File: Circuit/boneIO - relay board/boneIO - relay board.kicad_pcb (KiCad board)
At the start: 2 copper layers, 169 x 102 mm, 47 parts, among them J1 Screw_Terminal_01x04, J10 Screw_Terminal_01x04, J11 Screw_Terminal_01x04, J12 Conn_02x13_Odd_Even, J2 Screw_Terminal_01x04, J3 Screw_Terminal_01x04, J4 Screw_Terminal_01x04, J5 Screw_Terminal_01x04, J6 Screw_Terminal_01x04, J7 POWER RELAY, J8 Screw_Terminal_01x04, J9 Screw_Terminal_01x04, K1 RM85-2011-35-1005, K10 RM85-2011-35-1005, K11 RM85-2011-35-1005, K12 RM85-2011-35-1005, K13 RM85-2011-35-1005, K14 RM85-2011-35-1005, K15 RM85-2011-35-1005, K16 RM85-2011-35-1005, K17 RM85-2011-35-1005, K18 RM85-2011-35-1005, K19 RM85-2011-35-1005, K2 RM85-2011-35-1005, K20 RM85-2011-35-1005, K3 RM85-2011-35-1005, K4 RM85-2011-35-1005, K5 RM85-2011-35-1005, K6 RM85-2011-35-1005, K7 RM85-2011-35-1005, K8 RM85-2011-35-1005, K9 RM85-2011-35-1005, U1 ULN2803A, U2 ULN2803A, U3 ULN2803A, U4 MCP9808_MSOP

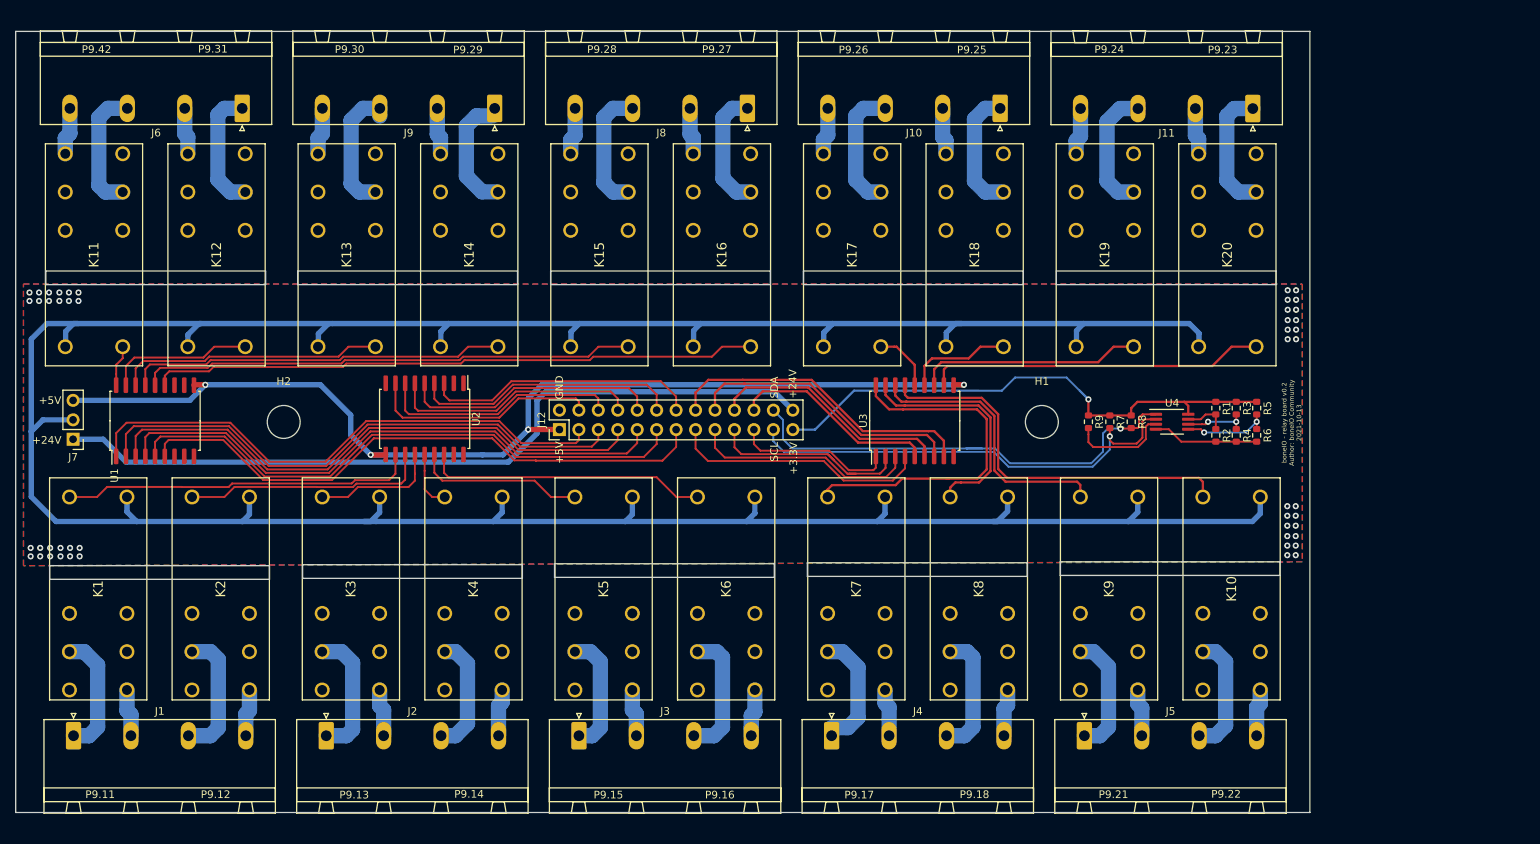
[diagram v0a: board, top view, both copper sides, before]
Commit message: Circuit Repo Cleanup
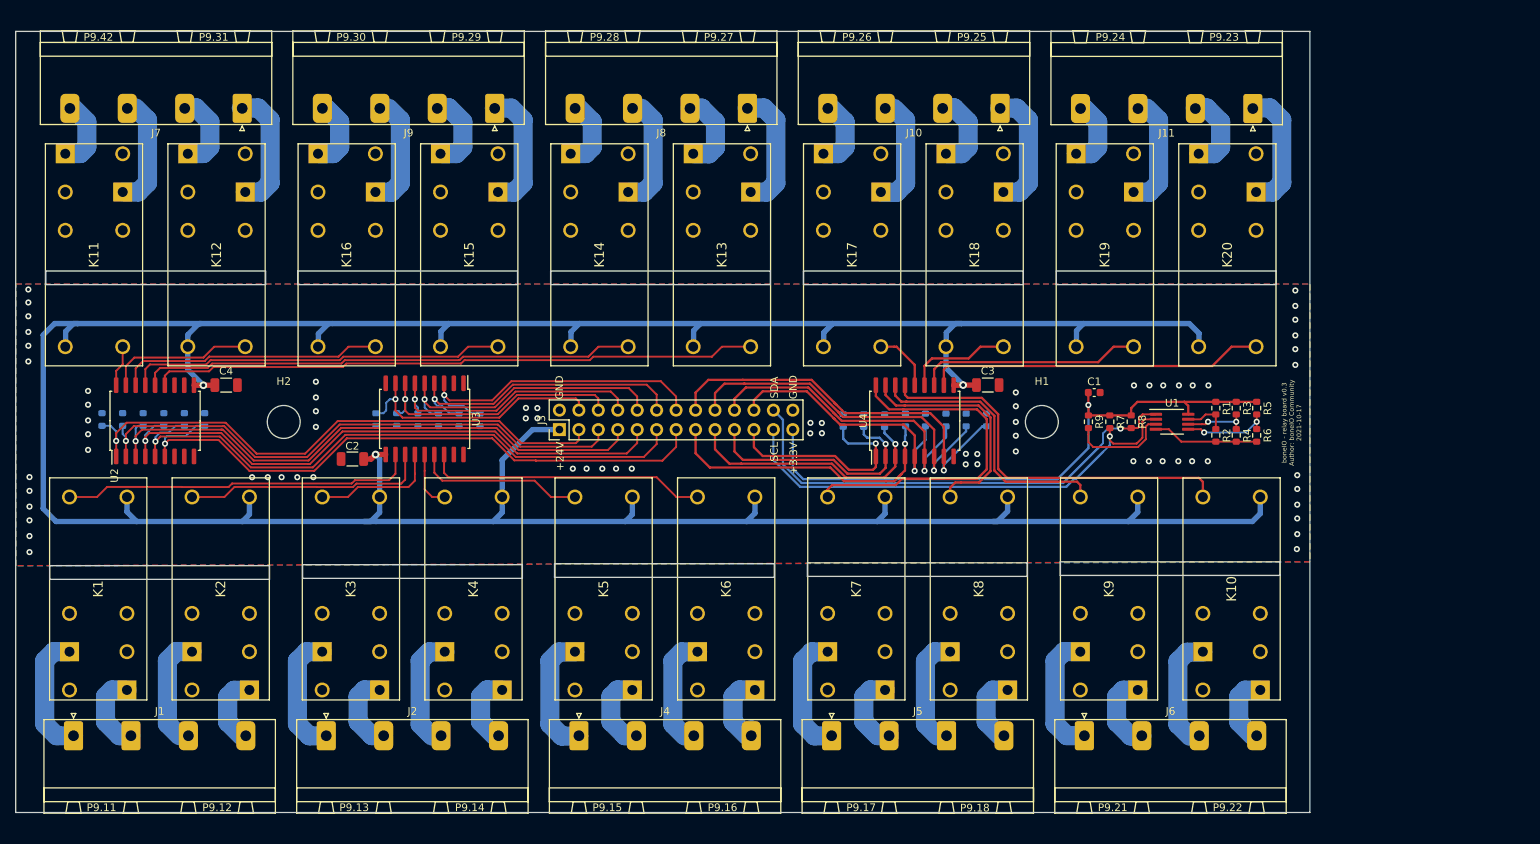
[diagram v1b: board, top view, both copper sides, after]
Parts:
- removed the J7 at (295.6, 317.0)
- added C1: 100n, Capacitor_SMD:C_0603_1608Metric, F.Cu at (429.0, 310.9)
- added C2: 4.7uF/50V, Capacitor_SMD:C_1206_3216Metric, F.Cu at (332.1, 319.5)
- added C3: 4.7uF/50V, Capacitor_SMD:C_1206_3216Metric, F.Cu at (415.1, 309.9)
- added C4: 4.7uF/50V, Capacitor_SMD:C_1206_3216Metric, F.Cu at (315.6, 309.9)
- added R10: 10k, Resistor_SMD:R_0603_1608Metric, B.Cu at (312.8, 314.4)
- added R11: 10k, Resistor_SMD:R_0603_1608Metric, B.Cu at (310.2, 314.4)
- added R12: 10k, Resistor_SMD:R_0603_1608Metric, B.Cu at (307.5, 314.4)
- added R13: 10k, Resistor_SMD:R_0603_1608Metric, B.Cu at (304.8, 314.4)
- added R14: 10k, Resistor_SMD:R_0603_1608Metric, B.Cu at (302.1, 314.4)
- added R15: 10k, Resistor_SMD:R_0603_1608Metric, B.Cu at (299.4, 314.4)
- added R16: 10k, Resistor_SMD:R_0603_1608Metric, B.Cu at (335.2, 314.4)
- added R17: 10k, Resistor_SMD:R_0603_1608Metric, B.Cu at (337.9, 314.4)
- added R18: 10k, Resistor_SMD:R_0603_1608Metric, B.Cu at (340.7, 314.4)
- added R19: 10k, Resistor_SMD:R_0603_1608Metric, B.Cu at (343.4, 314.4)
- added R20: 10k, Resistor_SMD:R_0603_1608Metric, B.Cu at (346.0, 314.4)
- added R21: 10k, Resistor_SMD:R_0603_1608Metric, B.Cu at (348.8, 314.4)
- added R22: 10k, Resistor_SMD:R_0603_1608Metric, B.Cu at (414.9, 314.4)
- added R23: 10k, Resistor_SMD:R_0603_1608Metric, B.Cu at (412.2, 314.4)
- added R24: 10k, Resistor_SMD:R_0603_1608Metric, B.Cu at (409.6, 314.4)
- added R25: 10k, Resistor_SMD:R_0603_1608Metric, B.Cu at (406.9, 314.4)
- added R26: 10k, Resistor_SMD:R_0603_1608Metric, B.Cu at (404.3, 314.4)
- added R27: 10k, Resistor_SMD:R_0603_1608Metric, B.Cu at (401.6, 314.5)
- added R28: 10k, Resistor_SMD:R_0603_1608Metric, B.Cu at (398.9, 314.5)
- added R29: 10k, Resistor_SMD:R_0603_1608Metric, B.Cu at (396.2, 314.5)
- renumbered J12 to J3, J3 to J4, J4 to J5, J5 to J6, J6 to J7, K16 to K13, K15 to K14, K14 to K15, K13 to K16, U4 to U1, U1 to U2, U2 to U3, U3 to U4
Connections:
- J3 pad 1: +5V -> +24V
- J3 pad 26: +24V -> GND
- K1 pad A2: VCC -> +24V
- K10 pad A2: VCC -> +24V
- K11 pad A2: VCC -> +24V
- K12 pad A2: VCC -> +24V
- K13 pad A2: VCC -> +24V
- K14 pad A2: VCC -> +24V
- K15 pad A2: VCC -> +24V
- K16 pad A2: VCC -> +24V
- K17 pad A2: VCC -> +24V
- K18 pad A2: VCC -> +24V
- K19 pad A2: VCC -> +24V
- K2 pad A2: VCC -> +24V
- K20 pad A2: VCC -> +24V
- K3 pad A2: VCC -> +24V
- K4 pad A2: VCC -> +24V
- K5 pad A2: VCC -> +24V
- K6 pad A2: VCC -> +24V
- K7 pad A2: VCC -> +24V
- K8 pad A2: VCC -> +24V
- K9 pad A2: VCC -> +24V
- U2 pad 10: +5V -> +24V
- U3 pad 10: +5V -> +24V
- U4 pad 10: +5V -> +24V
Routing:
- net VCC: track 415.8 -> 0.00 mm
- net +24V: track 102.6 -> 448.4 mm, vias 0 -> 3
- net +5V: track 138.1 -> 0.00 mm, vias 4 -> 0
- net K17: track 40.7 -> 52.5 mm, vias 0 -> 1
- net K19: track 31.4 -> 42.3 mm, vias 0 -> 1
- net K18: track 36.4 -> 47.0 mm, vias 0 -> 1
- net +3V3: track 69.9 -> 79.8 mm
- net K20: track 27.0 -> 36.4 mm, vias 0 -> 1
- net K10: track 21.6 -> 29.5 mm, vias 0 -> 1
- net K16: track 35.8 -> 41.8 mm, vias 0 -> 1
- net K6: track 77.3 -> 82.8 mm, vias 0 -> 1
- net Net-(J9-Pad2): track 5.10 -> 10.5 mm
- net Net-(J5-Pad2): track 5.14 -> 10.5 mm
- net K7: track 33.8 -> 39.0 mm, vias 0 -> 1
- net Net-(J11-Pad2): track 6.08 -> 10.5 mm
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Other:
- board text added: "boneIO - relay board v0.3 Author: boneIO Community 2021-10-17"
- board text removed: "+5V"
- board text removed: "boneIO - relay board v0.2 Author: boneIO Community 2021-10-13"

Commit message: Repo Sync for new people
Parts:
- removed C1: 100n, Capacitor_SMD:C_0603_1608Metric
- removed C2, C3, C4: 4.7uF/50V, Capacitor_SMD:C_1206_3216Metric
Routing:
- net +24V: track 448.4 -> 443.2 mm
- net K6: track 82.8 -> 83.8 mm
- net K3: track 75.3 -> 76.3 mm
- net K2: track 73.5 -> 74.5 mm
- net K5: track 79.9 -> 80.9 mm
- net K4: track 77.6 -> 78.6 mm
- net K1: track 73.6 -> 74.6 mm
- net GND: vias 72 -> 68
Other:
- board text added: "boneIO - relay board v0.2 Author: boneIO Community 2021-10-17"
- board text removed: "boneIO - relay board v0.3 Author: boneIO Community 2021-10-17"

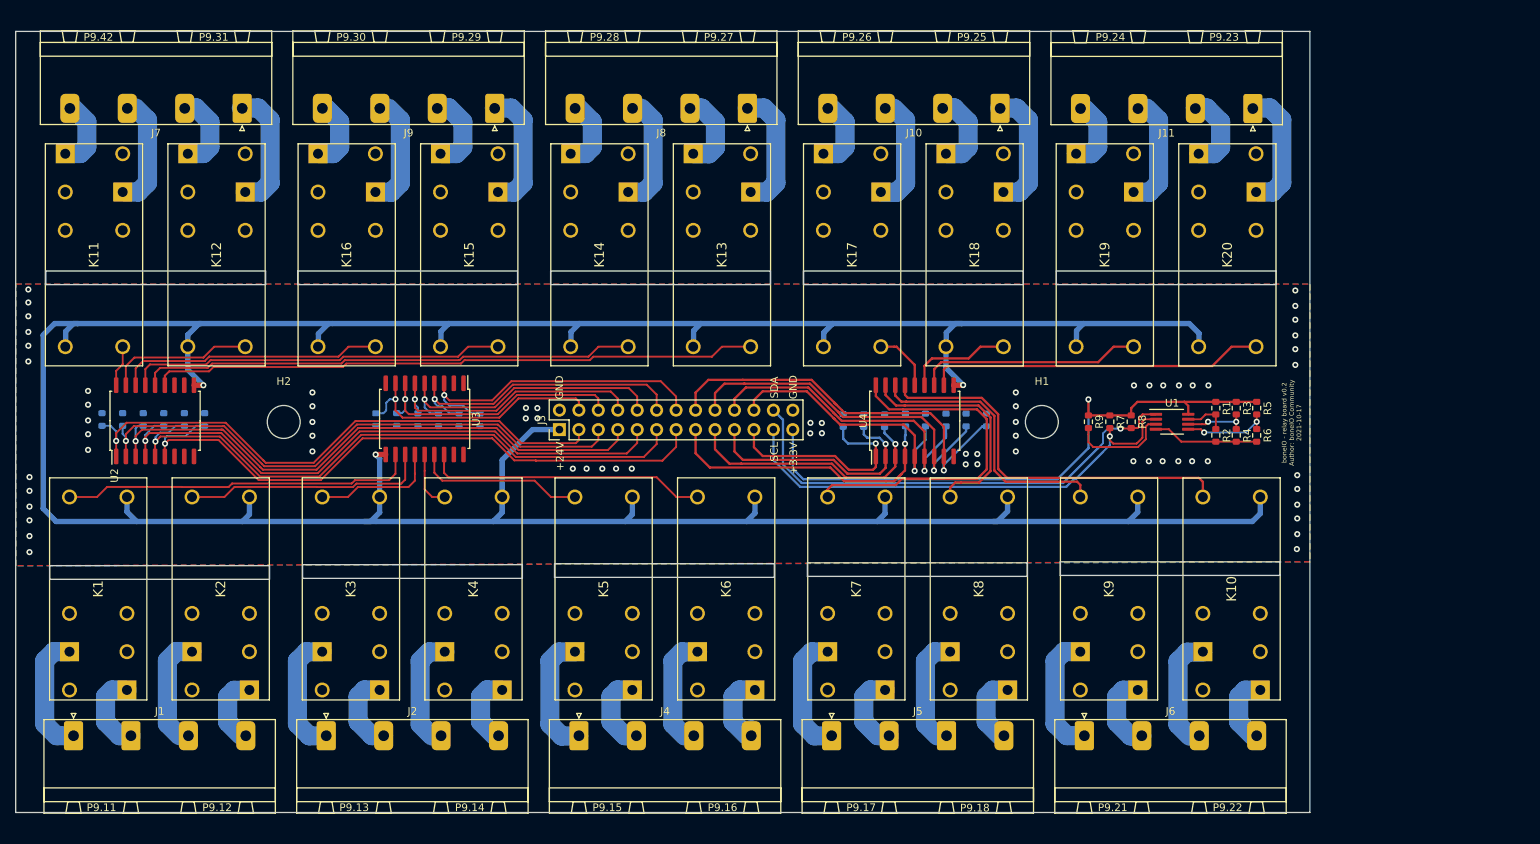
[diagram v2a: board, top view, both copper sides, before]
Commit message: Wykonana PCB RELAY RM85_v0.2
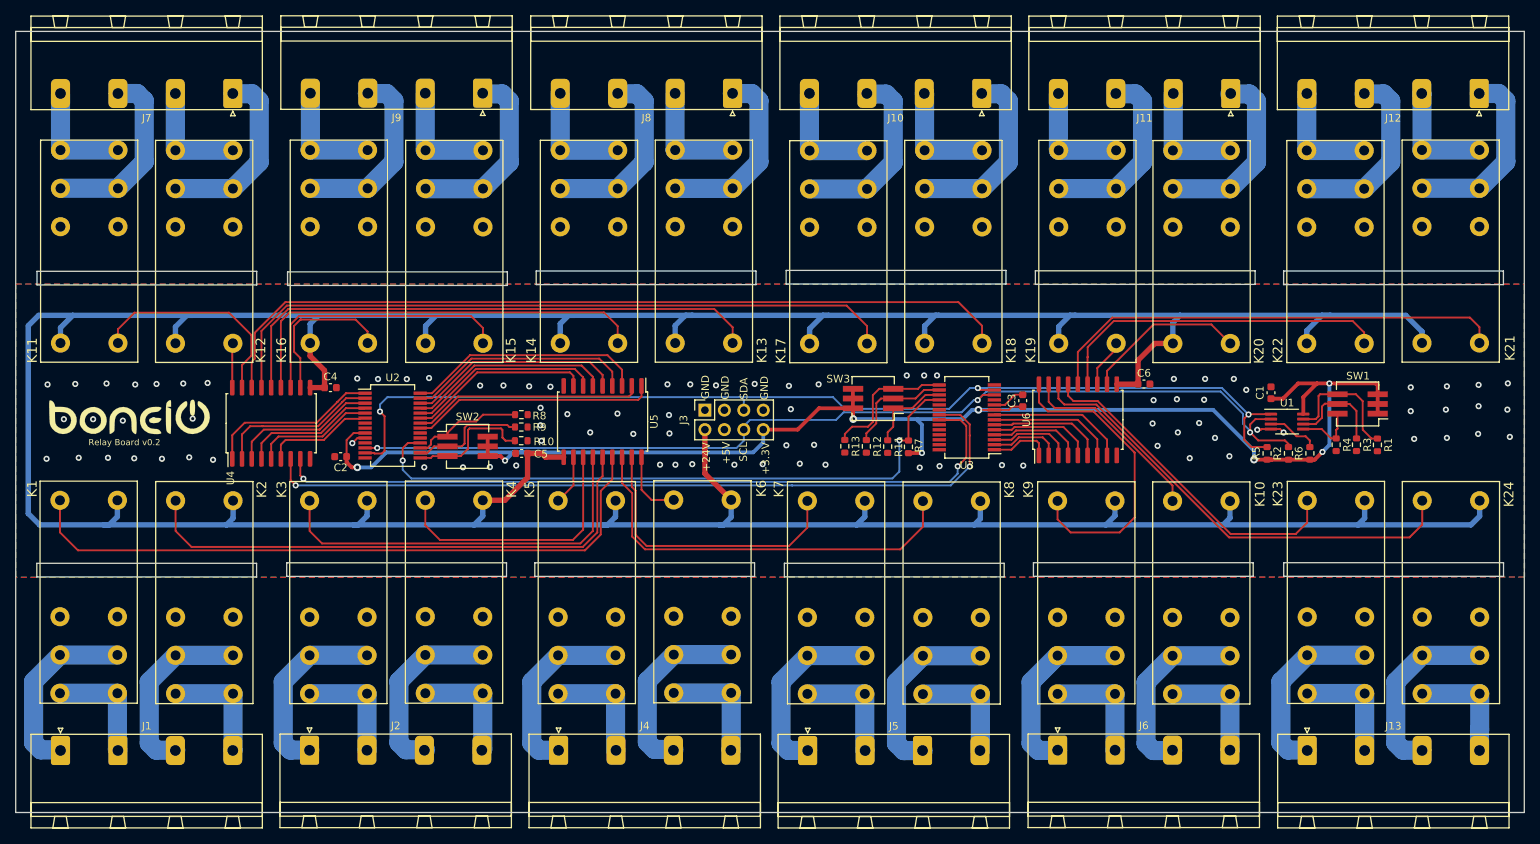
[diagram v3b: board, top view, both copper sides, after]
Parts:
- removed H1, H2: MountingHole, MountingHole:MountingHole_4.3mm_M4
- removed the R1 at (444.9, 312.9)
- removed R14, R15, R16, R17, R18, R19, R20, R21, R22, R23, R24, R25, R26, R27, R28, R29: 10k, Resistor_SMD:R_0603_1608Metric
- removed the R3 at (447.5, 312.9)
- removed the R5 at (450.2, 312.9)
- added C1: 100n, Capacitor_SMD:C_0603_1608Metric, F.Cu at (452.1, 310.9)
- added C2: 100n, Capacitor_SMD:C_0603_1608Metric, F.Cu at (330.6, 319.2)
- added C3: 100n, Capacitor_SMD:C_0603_1608Metric, F.Cu at (419.6, 311.9)
- added C4: 100n, Capacitor_SMD:C_0603_1608Metric, F.Cu at (329.2, 310.2)
- added C5: 100n, Capacitor_SMD:C_0603_1608Metric, F.Cu at (354.2, 318.8)
- added C6: 100n, Capacitor_SMD:C_0603_1608Metric, F.Cu at (435.5, 309.8)
- added G***: LOGO, Symbol:boneIO_LOGO_srednie, F.Cu at (303.0, 314.1)
- added J12: Screw_Terminal_01x04, Connector_Phoenix_GMSTB:PhoenixContact_GMSTBA_2,5_4-G_1x04_P7.50mm_Horizontal, F.Cu at (479.2, 271.8)
- added J13: Screw_Terminal_01x04, Connector_Phoenix_GMSTB:PhoenixContact_GMSTBA_2,5_4-G_1x04_P7.50mm_Horizontal, F.Cu at (456.8, 357.6)
- added K21: RM85-2011-35-1005, boneIO - RM85:RM852011351005_1, F.Cu at (479.3, 284.2)
- added K22: RM85-2011-35-1005, boneIO - RM85:RM852011351005_1, F.Cu at (464.2, 284.3)
- added K23: RM85-2011-35-1005, boneIO - RM85:RM852011351005_1, F.Cu at (456.8, 345.2)
- added K24: RM85-2011-35-1005, boneIO - RM85:RM852011351005_1, F.Cu at (471.8, 345.2)
- added R7: 4.7k, Resistor_SMD:R_0603_1608Metric, F.Cu at (404.7, 318.0)
- added R8: 0k, Resistor_SMD:R_0603_1608Metric, F.Cu at (354.2, 313.8)
- added R9: 0k, Resistor_SMD:R_0603_1608Metric, F.Cu at (354.2, 315.4)
- added SW1: SW_DIP_x03, Button_Switch_SMD:SW_DIP_SPSTx03_Slide_KingTek_DSHP03TJ_W5.25mm_P1.27mm_JPin, F.Cu at (463.4, 312.4)
- added SW2: SW_DIP_x03, Button_Switch_SMD:SW_DIP_SPSTx03_Slide_KingTek_DSHP03TJ_W5.25mm_P1.27mm_JPin, F.Cu at (347.1, 317.9)
- added SW3: SW_DIP_x03, Button_Switch_SMD:SW_DIP_SPSTx03_Slide_KingTek_DSHP03TJ_W5.25mm_P1.27mm_JPin, F.Cu at (400.1, 311.6)
- added U2: MCP23017_SS, Package_SO:SSOP-28_5.3x10.2mm_P0.65mm, F.Cu at (337.4, 315.2)
- added U3: MCP23017_SS, Package_SO:SSOP-28_5.3x10.2mm_P0.65mm, F.Cu at (412.3, 314.1)
- J3: value Conn_02x13_Odd_Even -> Conn_02x04_Odd_Even; footprint Connector_PinHeader_2.54mm:PinHeader_2x13_P2.54mm_Vertical -> Connector_PinSocket_2.54mm:PinSocket_2x04_P2.54mm_Vertical
- K1, K10, K11, K12, K13, K14, K15, K16, K17, K18, K19, K2, K20, K3, K4, K5, K6, K7, K8, K9: footprint RM85-2011-35-1005:RM852011351005 -> boneIO - RM85:RM852011351005_1
- R10, R11, R12, R13: value 10k -> 0k; moved to F.Cu
- moved R11 91.9 mm to (402.0, 317.9), turned to 270 degrees
- moved R12 91.8 mm to (399.2, 317.9), turned to 270 degrees
- moved R13 91.7 mm to (396.4, 317.9), turned to 270 degrees
- moved R10 41.4 mm to (354.2, 317.2), turned to 0 degrees
- moved R6 29.2 mm to (457.1, 318.8), turned to 90 degrees
- moved R2 23.7 mm to (454.3, 318.8), turned to 90 degrees
- moved U5 23.2 mm to (364.8, 314.7)
- moved U6 21.3 mm to (426.8, 314.4)
- moved R1 21.1 mm to (466.0, 317.7)
- moved J3 19.2 mm to (378.1, 313.2)
- moved R5 18.2 mm to (451.6, 318.8), turned to 90 degrees
- moved R3 15.7 mm to (463.2, 317.7)
- moved U4 15.2 mm to (321.5, 314.9)
- moved U1 15.0 mm to (454.2, 314.7)
- moved R4 10.4 mm to (460.6, 317.7)
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- renumbered R2 to R1, R7 to R2, R4 to R3, R6 to R4, R8 to R5, R9 to R6, U2 to U4, U3 to U5, U4 to U6
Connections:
- J3 pad 1: +24V -> GND
- J3 pad 2: GND -> +24V
- J3 pad 3: K1 -> GND
- J3 pad 4: K11 -> +5V
- J3 pad 5: K2 -> SDA
- J3 pad 6: K12 -> SCL
- J3 pad 7: K3 -> GND
- J3 pad 8: K13 -> +3V3
- K1 pad 14: Net-(K1-Pad14) -> Net-(J1-Pad2)
- K1 pad 21: Net-(K1-Pad21) -> Net-(J1-Pad1)
- K10 pad 14: Net-(K10-Pad14) -> Net-(J6-Pad4)
- K10 pad 21: Net-(K10-Pad21) -> Net-(J6-Pad3)
- K11 pad 14: Net-(K11-Pad14) -> Net-(J7-Pad4)
- K11 pad 21: Net-(K11-Pad21) -> Net-(J7-Pad3)
- K12 pad 14: Net-(K12-Pad14) -> Net-(J7-Pad2)
- K12 pad 21: Net-(K12-Pad21) -> Net-(J7-Pad1)
- K13 pad 14: Net-(K13-Pad14) -> Net-(J8-Pad2)
- K13 pad 21: Net-(K13-Pad21) -> Net-(J8-Pad1)
- K14 pad 14: Net-(K14-Pad14) -> Net-(J8-Pad4)
- K14 pad 21: Net-(K14-Pad21) -> Net-(J8-Pad3)
- K15 pad 14: Net-(K15-Pad14) -> Net-(J9-Pad2)
- K15 pad 21: Net-(K15-Pad21) -> Net-(J9-Pad1)
- K16 pad 14: Net-(K16-Pad14) -> Net-(J9-Pad4)
- K16 pad 21: Net-(K16-Pad21) -> Net-(J9-Pad3)
- K17 pad 14: Net-(K17-Pad14) -> Net-(J10-Pad4)
- K17 pad 21: Net-(K17-Pad21) -> Net-(J10-Pad3)
- K18 pad 14: Net-(K18-Pad14) -> Net-(J10-Pad2)
- K18 pad 21: Net-(K18-Pad21) -> Net-(J10-Pad1)
- K19 pad 14: Net-(K19-Pad14) -> Net-(J11-Pad4)
- K19 pad 21: Net-(K19-Pad21) -> Net-(J11-Pad3)
- K2 pad 14: Net-(K2-Pad14) -> Net-(J1-Pad4)
- K2 pad 21: Net-(K2-Pad21) -> Net-(J1-Pad3)
- K20 pad 14: Net-(K20-Pad14) -> Net-(J11-Pad2)
- K20 pad 21: Net-(K20-Pad21) -> Net-(J11-Pad1)
- K3 pad 14: Net-(K3-Pad14) -> Net-(J2-Pad2)
- K3 pad 21: Net-(K3-Pad21) -> Net-(J2-Pad1)
- K4 pad 14: Net-(K4-Pad14) -> Net-(J2-Pad4)
- K4 pad 21: Net-(K4-Pad21) -> Net-(J2-Pad3)
- K5 pad 14: Net-(K5-Pad14) -> Net-(J4-Pad2)
- K5 pad 21: Net-(K5-Pad21) -> Net-(J4-Pad1)
- K6 pad 14: Net-(K6-Pad14) -> Net-(J4-Pad4)
- K6 pad 21: Net-(K6-Pad21) -> Net-(J4-Pad3)
- K7 pad 14: Net-(K7-Pad14) -> Net-(J5-Pad2)
- K7 pad 21: Net-(K7-Pad21) -> Net-(J5-Pad1)
- K8 pad 14: Net-(K8-Pad14) -> Net-(J5-Pad4)
- K8 pad 21: Net-(K8-Pad21) -> Net-(J5-Pad3)
- K9 pad 14: Net-(K9-Pad14) -> Net-(J6-Pad2)
- K9 pad 21: Net-(K9-Pad21) -> Net-(J6-Pad1)
- R10 pad 1: K6 -> Net-(R10-Pad1)
- R11 pad 1: K5 -> Net-(R11-Pad1)
- R12 pad 1: K4 -> Net-(R12-Pad1)
- R13 pad 1: K3 -> Net-(R13-Pad1)
- U4 pad 11: Net-(U2-Pad11) -> RELAY13
- U4 pad 12: Net-(U2-Pad12) -> RELAY14
- U4 pad 13: RELAY16 -> RELAY15
- U4 pad 14: RELAY15 -> RELAY16
- U4 pad 15: RELAY14 -> RELAY17
- U4 pad 16: RELAY13 -> RELAY18
- U4 pad 17: RELAY12 -> RELAY11
- U4 pad 18: RELAY11 -> RELAY12
- U4 pad 7: Net-(U2-Pad7) -> K21
- U4 pad 8: Net-(U2-Pad8) -> K22
- U5 pad 1: Net-(U3-Pad1) -> K23
- U5 pad 11: RELAY1 -> RELAY5
- U5 pad 12: RELAY2 -> RELAY4
- U5 pad 14: RELAY4 -> RELAY2
- U5 pad 15: RELAY5 -> RELAY1
- U5 pad 16: RELAY6 -> RELAY8
- U5 pad 17: Net-(U3-Pad17) -> RELAY7
- U5 pad 18: Net-(U3-Pad18) -> RELAY6
- U5 pad 2: Net-(U3-Pad2) -> K24
- U6 pad 13: RELAY18 -> RELAY22
- U6 pad 14: RELAY17 -> RELAY21
- U6 pad 15: RELAY10 -> RELAY23
- U6 pad 16: RELAY9 -> RELAY24
- U6 pad 17: RELAY8 -> RELAY10
- U6 pad 18: RELAY7 -> RELAY9
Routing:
- net +3V3: track 79.6 -> 199.7 mm, vias 1 -> 8
- net K21: track 0.00 -> 102.8 mm, vias 0 -> 2
- net K22: track 0.00 -> 99.4 mm, vias 0 -> 2
- net +24V: track 443.2 -> 542.3 mm, vias 3 -> 0
- net RELAY18: track 13.9 -> 107.5 mm
- net RESET_MCP: track 0.00 -> 84.4 mm, vias 0 -> 2
- net RELAY17: track 8.06 -> 91.3 mm
- net SDA: track 62.6 -> 140.3 mm, vias 1 -> 3
- net SCL: track 63.5 -> 135.4 mm, vias 1 -> 3
- net K6: track 83.8 -> 14.3 mm, vias 1 -> 0
- net K5: track 80.9 -> 15.9 mm, vias 1 -> 0
- net K4: track 78.6 -> 17.5 mm, vias 1 -> 0
- net RELAY21: track 0.00 -> 61.1 mm
- net RELAY24: track 0.00 -> 60.7 mm
- net K3: track 76.3 -> 19.1 mm, vias 1 -> 0
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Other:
- board size 169 x 102 mm -> 197 x 102 mm
- board text added: "+5V"
- board text added: "Relay Board v0.2"
- board text removed: "P9.11"
- board text removed: "P9.12"
- board text removed: "P9.13"
- board text removed: "P9.14"
- board text removed: "P9.15"
- board text removed: "P9.16"
- board text removed: "P9.17"
- board text removed: "P9.18"
- board text removed: "P9.21"
- board text removed: "P9.22"
- board text removed: "P9.23"
- board text removed: "P9.24"
- board text removed: "P9.25"
- board text removed: "P9.26"
- board text removed: "P9.27"
- board text removed: "P9.28"
- board text removed: "P9.29"
- board text removed: "P9.30"
- board text removed: "P9.31"
- board text removed: "P9.42"
- board text removed: "boneIO - relay board v0.2 Author: boneIO Community 2021-10-17"

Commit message: 01.11.2021
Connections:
- J3 pad 5: SDA -> GND
- J3 pad 6: SCL -> +3V3
- J3 pad 7: GND -> SDA
- J3 pad 8: +3V3 -> SCL
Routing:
- net +3V3: track 199.7 -> 203.7 mm, vias 8 -> 10
- net SCL: track 135.4 -> 136.1 mm
